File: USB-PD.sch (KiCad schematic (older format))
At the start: 32 parts, among them J11 WE_632723300011, Q7 IRF7404TRPBF, U18 STUSB4500QTR

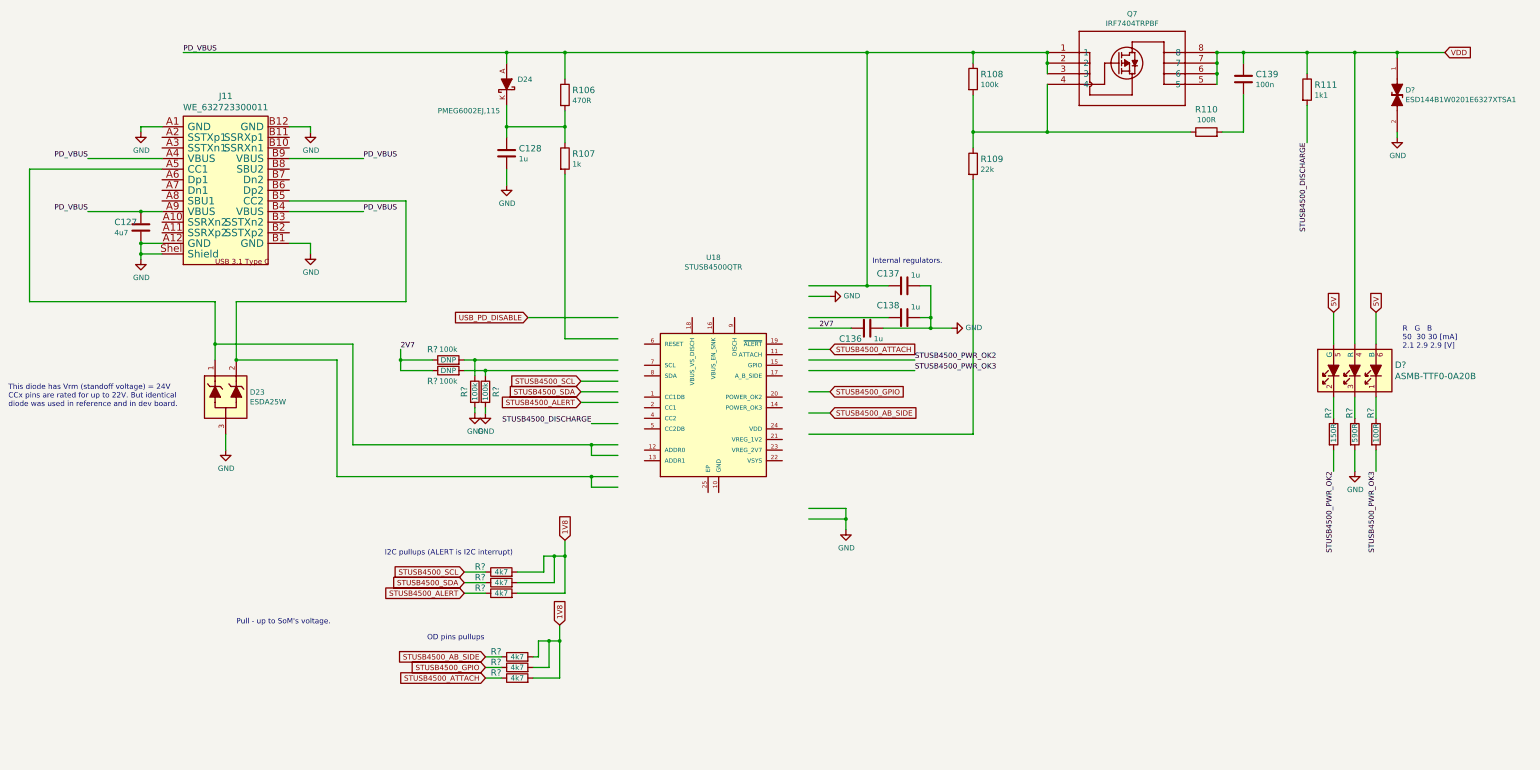
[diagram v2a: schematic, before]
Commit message: Cleanup USB-PD.sch, tweak STUSB and RGB led symbols for cleaner schematic
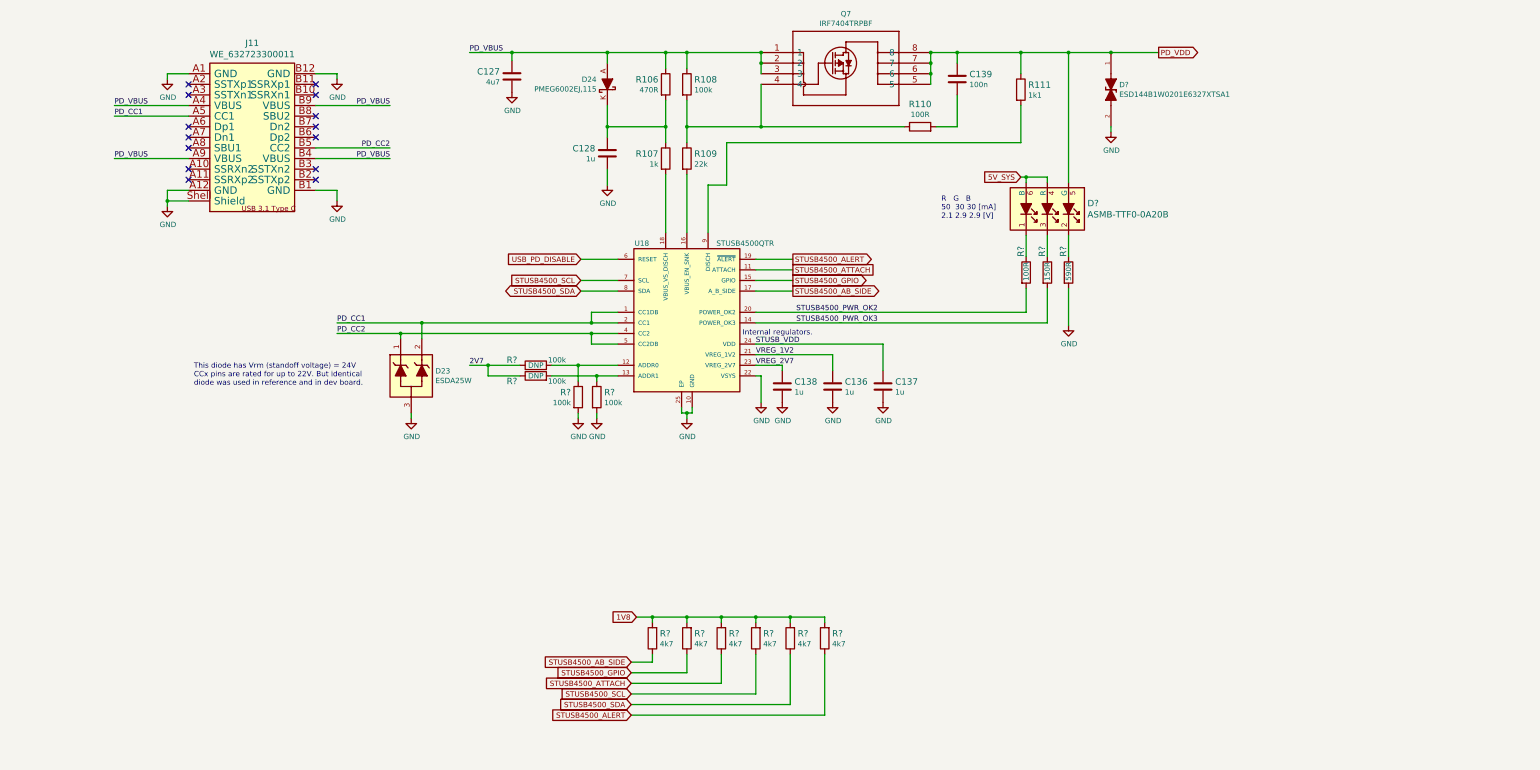
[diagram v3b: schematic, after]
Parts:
- removed D?: ESD144B1W0201E6327XTSA1, sa800u-baseboard-hw-footprints:ESD144B1W0201E6327XTSA1, symbol sa800u-baseboard-hw:ESD144B1W0201E6327XTSA1
- removed R? (x3): R_4k7_0402, sa800u-baseboard-hw-footprints:0402-res, symbol sa800u-baseboard-hw:R_4k7_0402
- added D?: ESD144B1W0201E6327XTSA1, antmicro-footprints:ESD144B1W0201E6327XTSA1, symbol antmicroTVSDiodes:ESD144B1W0201E6327XTSA1
- added R? (x3): R_4k7_0402, sa800u-baseboard-hw-footprints:0402-res, symbol sa800u-baseboard-hw:R_4k7_0402
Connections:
- net labels added: 5V_SYS, PD_CC1, PD_CC2, PD_VDD, STUSB_VDD, VREG_1V2, VREG_2V7
- net labels removed: 5V, STUSB4500_DISCHARGE, VDD
- wire segments 148 -> 140
- no-connect marks 0 -> 14
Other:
- note removed: "I2C pullups (ALERT is I2C interrupt)"
- note removed: "OD pins pullups"
- note removed: "Pull - up to SoM's voltage."
- moved on the sheet: C127, C128, C136, C137, C138, C139, D23, D24, D?, J11, Q7, R106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

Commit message: Annotate parts
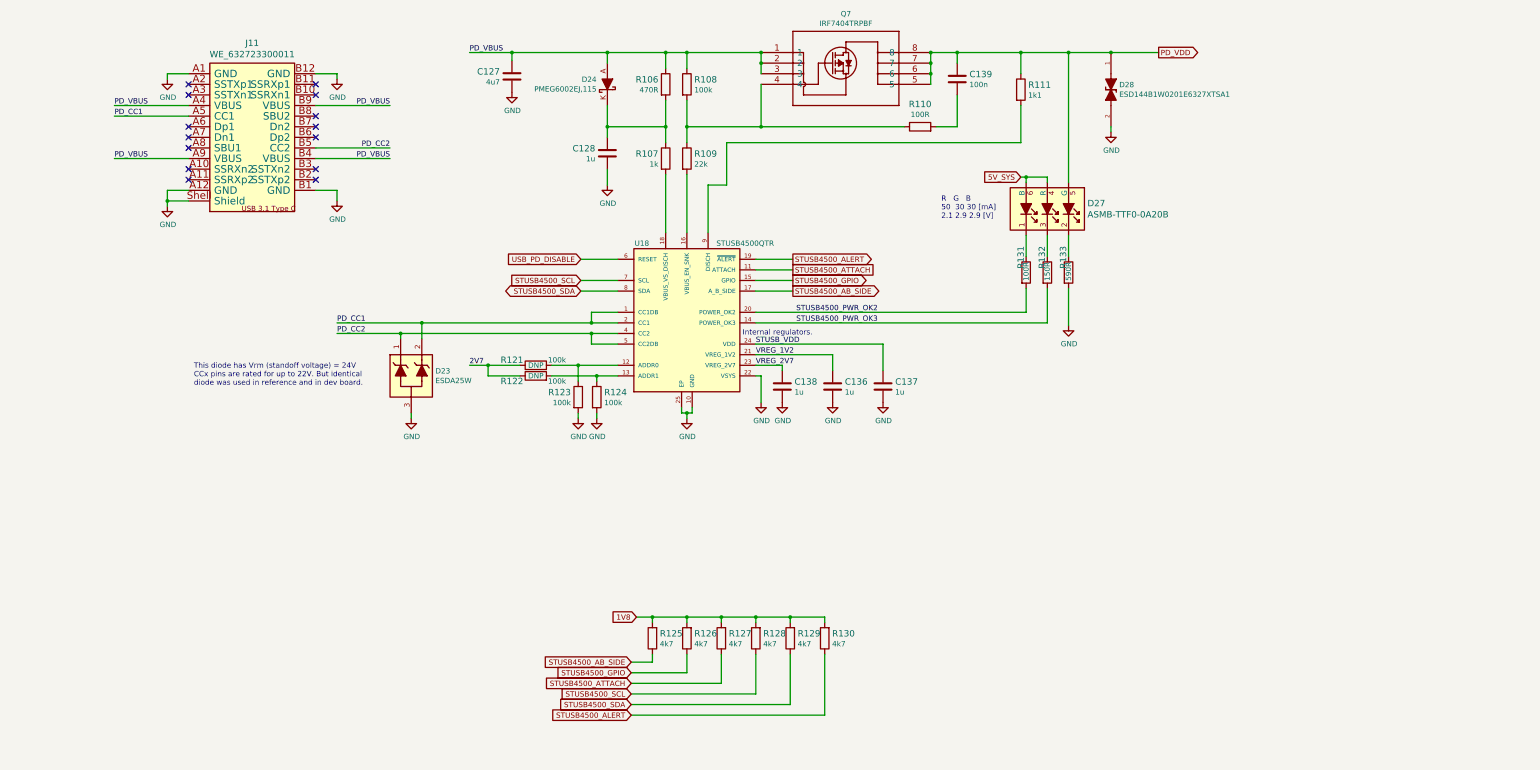
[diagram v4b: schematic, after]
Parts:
- gave numbers to parts that had none: 15
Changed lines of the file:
@@
 2V7
 $Comp
-L sa800u-baseboard-hw:R_100k_0402 R?
+L sa800u-baseboard-hw:R_100k_0402 R121
 U 1 1 61EEDDB8
 P 5925 4700
-F 0 "R?" H 5700 4750 60  0000 C CNN
+F 0 "R121" H 5700 4750 60  0000 C CNN
 F 1 "R_100k_0402" H 5925 4550 60  0001 C CNN
 F 2 "sa800u-baseboard-hw-footprints:0402-res" H 6125 4900 60  0001 L CNN
@@
 	5775 4700 5475 4700
 $Comp
-L sa800u-baseboard-hw:R_100k_0402 R?
+L sa800u-baseboard-hw:R_100k_0402 R122
 U 1 1 61EEE353
 P 5925 4800
-F 0 "R?" H 5700 4750 60  0000 C CNN
+F 0 "R122" H 5700 4750 60  0000 C CNN
 F 1 "R_100k_0402" H 5925 4650 60  0001 C CNN
 F 2 "sa800u-baseboard-hw-footprints:0402-res" H 6125 5000 60  0001 L CNN
@@
 	6500 4800 6500 4850
 $Comp
-L sa800u-baseboard-hw:GND #PWR?
+L sa800u-baseboard-hw:GND #PWR0178
 U 1 1 61EF35F3
 P 6325 5200
-F 0 "#PWR?" H 6325 4950 50  0001 C CNN
+F 0 "#PWR0178" H 6325 4950 50  0001 C CNN
 F 1 "GND" H 6330 5027 50  0000 C CNN
 F 2 "" H 6325 5200 50  0001 C CNN
@@
 $EndComp
 $Comp
-L sa800u-baseboard-hw:GND #PWR?
+L sa800u-baseboard-hw:GND #PWR0180
 U 1 1 61EF3823
 P 6500 5200
-F 0 "#PWR?" H 6500 4950 50  0001 C CNN
+F 0 "#PWR0180" H 6500 4950 50  0001 C CNN
 F 1 "GND" H 6505 5027 50  0000 C CNN
 F 2 "" H 6500 5200 50  0001 C CNN
@@
 $EndComp
 $Comp
-L sa800u-baseboard-hw:R_100k_0402 R?
+L sa800u-baseboard-hw:R_100k_0402 R123
 U 1 1 61EF8DE3
 P 6325 5000
-F 0 "R?" V 6280 4931 60  0000 R CNN
+F 0 "R123" V 6280 4931 60  0000 R CNN
 F 1 "R_100k_0402" H 6325 4850 60  0001 C CNN
 F 2 "sa800u-baseboard-hw-footprints:0402-res" H 6525 5200 60  0001 L CNN
@@
 	6325 5150 6325 5200
 $Comp
-L sa800u-baseboard-hw:R_100k_0402 R?
+L sa800u-baseboard-hw:R_100k_0402 R124
 U 1 1 61F02819
 P 6500 5000
-F 0 "R?" V 6455 5070 60  0000 L CNN
+F 0 "R124" V 6455 5070 60  0000 L CNN
 F 1 "R_100k_0402" H 6500 4850 60  0001 C CNN
 F 2 "sa800u-baseboard-hw-footprints:0402-res" H 6700 5200 60  0001 L CNN
@@
 	6500 5150 6500 5200
 $Comp
-L sa800u-baseboard-hw:GND #PWR?
+L sa800u-baseboard-hw:GND #PWR0213
 U 1 1 61F1871C
 P 7350 5200
-F 0 "#PWR?" H 7350 4950 50  0001 C CNN
+F 0 "#PWR0213" H 7350 4950 50  0001 C CNN
 F 1 "GND" H 7355 5027 50  0000 C CNN
 F 2 "" H 7350 5200 50  0001 C CNN
@@
 	7025 7075 6875 7075
 $Comp
-L sa800u-baseboard-hw:R_4k7_0402 R?
+L sa800u-baseboard-hw:R_4k7_0402 R125
 U 1 1 62072163
 P 7025 7275
-F 0 "R?" V 7070 7205 60  0000 R CNN
+F 0 "R125" V 7070 7205 60  0000 R CNN
 F 1 "R_4k7_0402" H 7025 7125 60  0001 C CNN
 F 2 "sa800u-baseboard-hw-footprints:0402-res" H 7225 7475 60  0001 L CNN
@@
 $EndComp
 $Comp
-L sa800u-baseboard-hw:R_4k7_0402 R?
+L sa800u-baseboard-hw:R_4k7_0402 R126
 U 1 1 62072928
 P 7350 7275
-F 0 "R?" V 7395 7205 60  0000 R CNN
+F 0 "R126" V 7395 7205 60  0000 R CNN
 F 1 "R_4k7_0402" H 7350 7125 60  0001 C CNN
 F 2 "sa800u-baseboard-hw-footprints:0402-res" H 7550 7475 60  0001 L CNN
@@
 $EndComp
 $Comp
-L sa800u-baseboard-hw:R_4k7_0402 R?
+L sa800u-baseboard-hw:R_4k7_0402 R127
 U 1 1 62072AB9
 P 7675 7275
-F 0 "R?" V 7720 7205 60  0000 R CNN
+F 0 "R127" V 7720 7205 60  0000 R CNN
 F 1 "R_4k7_0402" H 7675 7125 60  0001 C CNN
 F 2 "sa800u-baseboard-hw-footprints:0402-res" H 7875 7475 60  0001 L CNN
@@
 	8050 4800 8050 5050
 $Comp
-L sa800u-baseboard-hw:GND #PWR?
+L sa800u-baseboard-hw:GND #PWR0214
 U 1 1 62BDA9D9
 P 8050 5050
-F 0 "#PWR?" H 8050 4800 50  0001 C CNN
+F 0 "#PWR0214" H 8050 4800 50  0001 C CNN
 F 1 "GND" H 8055 4877 50  0000 C CNN
 F 2 "" H 8050 5050 50  0001 C CNN
@@
 	9200 4500 9200 4750
 $Comp
-L sa800u-baseboard-hw:GND #PWR?
+L sa800u-baseboard-hw:GND #PWR0227
 U 1 1 62C0DF1E
 P 8250 5050
-F 0 "#PWR?" H 8250 4800 50  0001 C CNN
+F 0 "#PWR0227" H 8250 4800 50  0001 C CNN
 F 1 "GND" H 8255 4877 50  0000 C CNN
 F 2 "" H 8250 5050 50  0001 C CNN
@@
 $EndComp
 $Comp
-L sa800u-baseboard-hw:GND #PWR?
+L sa800u-baseboard-hw:GND #PWR0228
 U 1 1 62C13750
 P 8725 5050
-F 0 "#PWR?" H 8725 4800 50  0001 C CNN
+F 0 "#PWR0228" H 8725 4800 50  0001 C CNN
 F 1 "GND" H 8730 4877 50  0000 C CNN
 F 2 "" H 8725 5050 50  0001 C CNN
@@
 $EndComp
 $Comp
-L sa800u-baseboard-hw:GND #PWR?
+L sa800u-baseboard-hw:GND #PWR0229
 U 1 1 62C18F8E
 P 9200 5050
-F 0 "#PWR?" H 9200 4800 50  0001 C CNN
+F 0 "#PWR0229" H 9200 4800 50  0001 C CNN
 F 1 "GND" H 9205 4877 50  0000 C CNN
 F 2 "" H 9200 5050 50  0001 C CNN
@@
 	6825 7700 7675 7700
 $Comp
-L sa800u-baseboard-hw:R_4k7_0402 R?
+L sa800u-baseboard-hw:R_4k7_0402 R128
 U 1 1 62F55A66
 P 8000 7275
-F 0 "R?" V 8045 7205 60  0000 R CNN
+F 0 "R128" V 8045 7205 60  0000 R CNN
 F 1 "R_4k7_0402" H 8000 7125 60  0001 C CNN
 F 2 "sa800u-baseboard-hw-footprints:0402-res" H 8200 7475 60  0001 L CNN
@@
 $EndComp
 $Comp
-L sa800u-baseboard-hw:R_4k7_0402 R?
+L sa800u-baseboard-hw:R_4k7_0402 R129
 U 1 1 62F55A6F
 P 8325 7275
-F 0 "R?" V 8370 7205 60  0000 R CNN
+F 0 "R129" V 8370 7205 60  0000 R CNN
 F 1 "R_4k7_0402" H 8325 7125 60  0001 C CNN
 F 2 "sa800u-baseboard-hw-footprints:0402-res" H 8525 7475 60  0001 L CNN
@@
 Connection ~ 8000 7075
 $Comp
-L sa800u-baseboard-hw:R_4k7_0402 R?
+L sa800u-baseboard-hw:R_4k7_0402 R130
 U 1 1 62F5B4FE
 P 8650 7275
-F 0 "R?" V 8695 7205 60  0000 R CNN
+F 0 "R130" V 8695 7205 60  0000 R CNN
 F 1 "R_4k7_0402" H 8650 7125 60  0001 C CNN
 F 2 "sa800u-baseboard-hw-footprints:0402-res" H 8850 7475 60  0001 L CNN
@@
 	10500 2925 10550 2925
 $Comp
-L sa800u-baseboard-hw:ASMB-TTF0-0A20B D?
+L sa800u-baseboard-hw:ASMB-TTF0-0A20B D27
 U 1 1 620BAED1
 P 10750 3225
-F 0 "D?" V 10697 3603 60  0000 L CNN
+F 0 "D27" V 10697 3603 60  0000 L CNN
 F 1 "ASMB-TTF0-0A20B" V 10803 3603 60  0000 L CNN
 F 2 "sa800u-baseboard-hw-footprints:PLCC6_3.5x3.7mm" H 10350 2525 60  0001 L CNN
@@
 $EndComp
 $Comp
-L sa800u-baseboard-hw:R_100R_0402 R?
+L sa800u-baseboard-hw:R_100R_0402 R131
 U 1 1 6219BF48
 P 10550 3825
-F 0 "R?" H 10300 3775 60  0000 L CNN
+F 0 "R131" H 10300 3775 60  0000 L CNN
 F 1 "R_100R_0402" H 10550 3675 60  0001 C CNN
 F 2 "sa800u-baseboard-hw-footprints:0402-res" H 10750 4025 60  0001 L CNN
@@
 $EndComp
 $Comp
-L sa800u-baseboard-hw:R_150R_0402 R?
+L sa800u-baseboard-hw:R_150R_0402 R132
 U 1 1 62198F27
 P 10750 3825
-F 0 "R?" H 10500 3775 60  0000 L CNN
+F 0 "R132" H 10500 3775 60  0000 L CNN
 F 1 "R_150R_0402" H 10750 3675 60  0001 C CNN
 F 2 "sa800u-baseboard-hw-footprints:0402-res" H 10950 4025 60  0001 L CNN
@@
 	10750 3475 10750 3675
 $Comp
-L sa800u-baseboard-hw:GND #PWR?
+L sa800u-baseboard-hw:GND #PWR0230
 U 1 1 62113B31
 P 10950 4325
-F 0 "#PWR?" H 10950 4075 50  0001 C CNN
+F 0 "#PWR0230" H 10950 4075 50  0001 C CNN
 F 1 "GND" H 10955 4152 50  0000 C CNN
 F 2 "" H 10950 4325 50  0001 C CNN
@@
 	10950 3675 10950 3475
 $Comp
-L sa800u-baseboard-hw:R_590R_0402 R?
+L sa800u-baseboard-hw:R_590R_0402 R133
 U 1 1 621057A9
 P 10950 3825
-F 0 "R?" H 10700 3775 60  0000 L CNN
+F 0 "R133" H 10700 3775 60  0000 L CNN
 F 1 "R_590R_0402" H 10950 3675 60  0001 C CNN
 F 2 "sa800u-baseboard-hw-footprints:0402-res" H 11150 4025 60  0001 L CNN
@@
 NoConn ~ 3850 2150
 $Comp
-L antmicroTVSDiodes:ESD144B1W0201E6327XTSA1 D?
+L antmicroTVSDiodes:ESD144B1W0201E6327XTSA1 D28
 U 1 1 630E4F56
 P 11350 2100
-F 0 "D?" V 11304 2178 50  0000 L CNN
+F 0 "D28" V 11304 2178 50  0000 L CNN
 F 1 "ESD144B1W0201E6327XTSA1" V 11395 2178 50  0000 L CNN
 F 2 "antmicro-footprints:ESD144B1W0201E6327XTSA1" H 11350 2100 50  0001 C CNN
@@
 	11350 2450 11350 2500
 $Comp
-L sa800u-baseboard-hw:GND #PWR?
+L sa800u-baseboard-hw:GND #PWR0231
 U 1 1 61EDB438
 P 11350 2500
-F 0 "#PWR?" H 11350 2250 50  0001 C CNN
+F 0 "#PWR0231" H 11350 2250 50  0001 C CNN
 F 1 "GND" H 11355 2327 50  0000 C CNN
 F 2 "" H 11350 2500 50  0001 C CNN
@@
 	5700 1750 6600 1750
 $Comp
-L sa800u-baseboard-hw:GND #PWR?
+L sa800u-baseboard-hw:GND #PWR0232
 U 1 1 6311B6F5
 P 5700 2125
-F 0 "#PWR?" H 5700 1875 50  0001 C CNN
+F 0 "#PWR0232" H 5700 1875 50  0001 C CNN
 F 1 "GND" H 5705 1952 50  0000 C CNN
 F 2 "" H 5700 2125 50  0001 C CNN

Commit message: Loclib
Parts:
- D28: footprint antmicro-footprints:ESD144B1W0201E6327XTSA1 -> sa800u-baseboard-hw-footprints:ESD144B1W0201E6327XTSA1; symbol antmicroTVSDiodes:ESD144B1W0201E6327XTSA1 -> sa800u-baseboard-hw:ESD144B1W0201E6327XTSA1
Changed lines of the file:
@@
 NoConn ~ 3850 2150
 $Comp
-L antmicroTVSDiodes:ESD144B1W0201E6327XTSA1 D28
+L sa800u-baseboard-hw:ESD144B1W0201E6327XTSA1 D28
 U 1 1 630E4F56
 P 11350 2100
 F 0 "D28" V 11304 2178 50  0000 L CNN
 F 1 "ESD144B1W0201E6327XTSA1" V 11395 2178 50  0000 L CNN
-F 2 "antmicro-footprints:ESD144B1W0201E6327XTSA1" H 11350 2100 50  0001 C CNN
+F 2 "sa800u-baseboard-hw-footprints:ESD144B1W0201E6327XTSA1" H 11350 2100 50  0001 C CNN
 F 3 "https://www.infineon.com/dgdl/Infineon-ESD144-B1-W0201-DataSheet-v02_00-EN.pdf?fileId=5546d462677d0f4601679886a2a8707c" H 11350 2100 50  0001 C CNN
 F 4 "ESD144B1W0201E6327XTSA1" H 11350 2100 50  0001 C CNN "MPN"
